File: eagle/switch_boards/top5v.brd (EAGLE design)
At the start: 72.1 x 41.9 mm, 9 parts

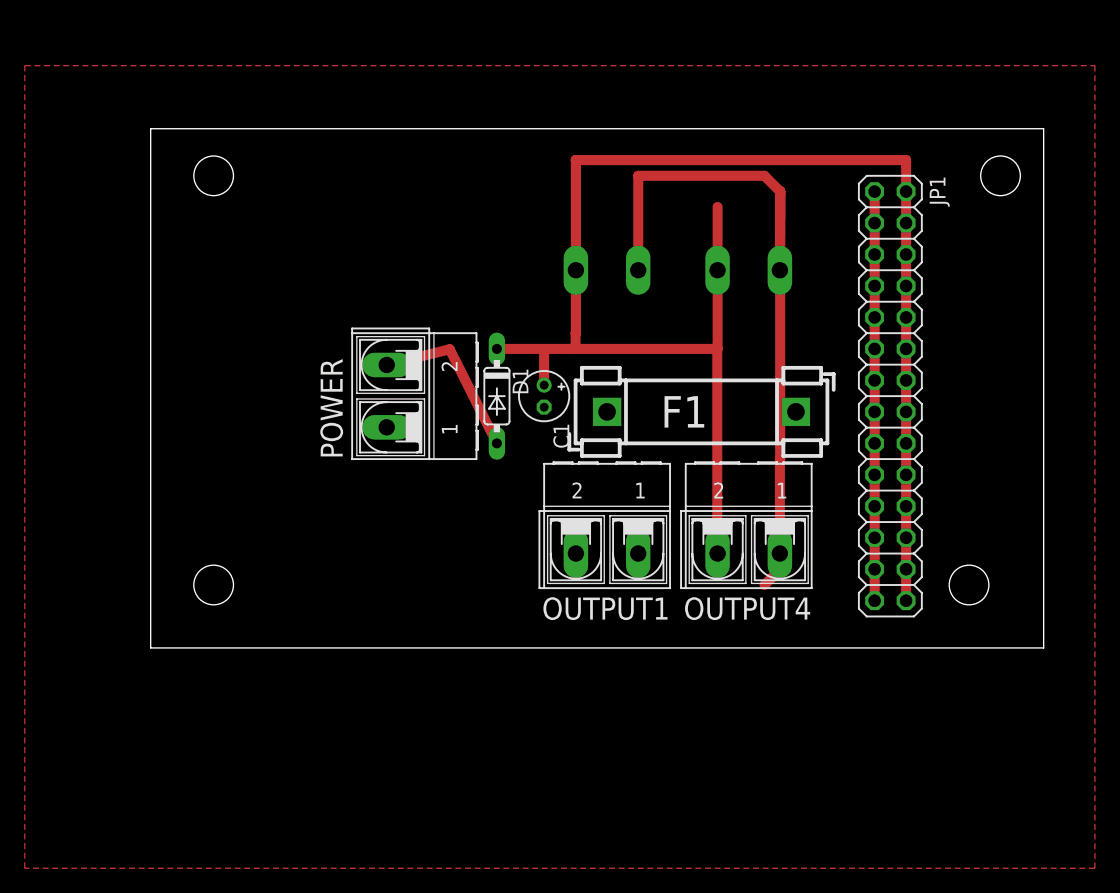
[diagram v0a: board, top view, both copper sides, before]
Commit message: switch board for 5v
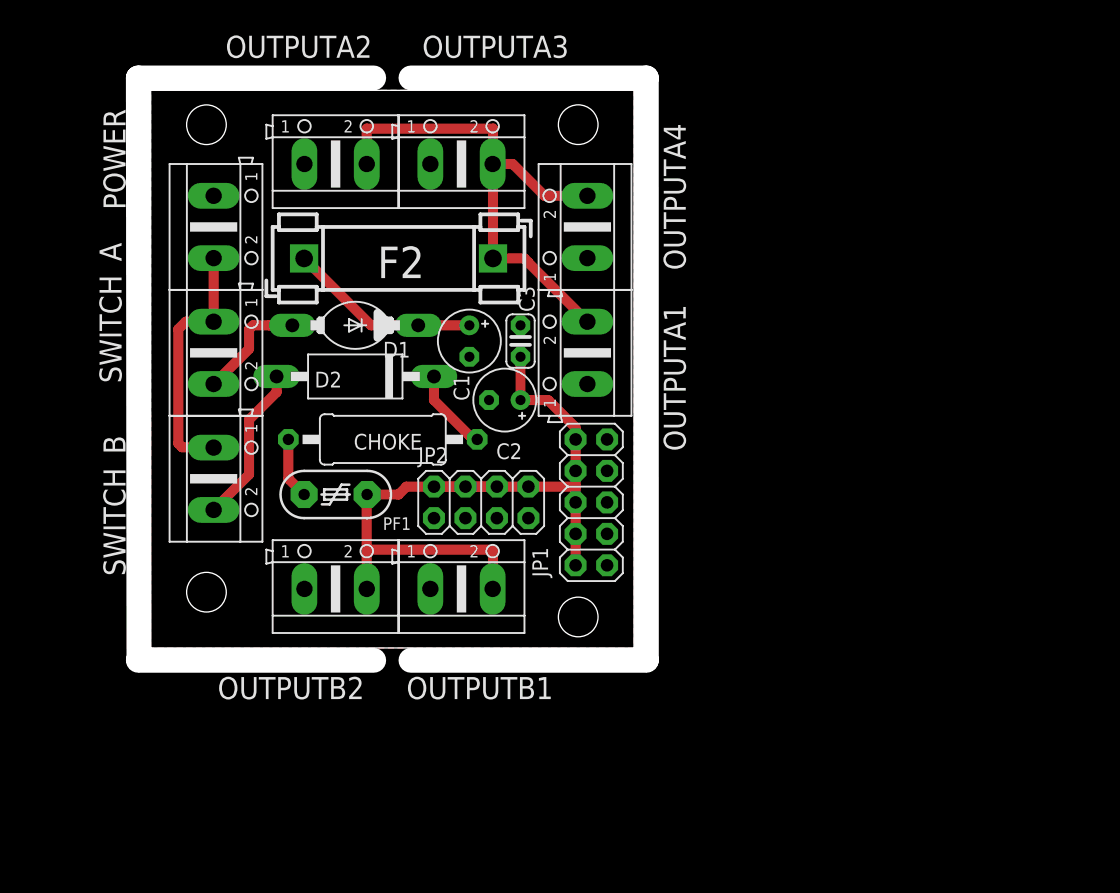
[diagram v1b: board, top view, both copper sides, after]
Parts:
- removed F1: FUSEBLANK_5X20MM, fuse:FUSE_HOLDER_5X20MM
- removed OUTPUT1, OUTPUT2, OUTPUT3, OUTPUT4: 5V, con-ptr500:AK500/2-H
- added C2: (no value), rcl:E2,5-5
- added C3: (no value), resistor:C025-024X044
- added CHOKE: 22uH, resistor:0411/15
- added D2: 1N5060GP, diode:DO15-12
- added F2: FUSEBLANK_5X20MM, fuse:FUSE_HOLDER_5X20MM
- added JP2: (no value), pinhead:2X04
- added OUTPUTA1, OUTPUTA2, OUTPUTA3, OUTPUTA4, OUTPUTB1, OUTPUTB2, SWITCH_A, SWITCH_B: 5V, con-ptr500:AK500/2
- added PF1: PTC-MF-5,1B, polyswitch:MF-5/1B
- C1: device resistor:E1,8-4 -> rcl:E2,5-5
- D1: value 1N4148DO35-7 -> 1N5059; device diode:DO35-7 -> diode:DO204-10
- JP1: device pinhead:2X14 -> pinhead:2X05
- POWER: device con-ptr500:AK500/2-H -> con-ptr500:AK500/2
- moved JP1 25.6 mm to (35.6, 11.7), turned to 90 degrees
- moved POWER 19.5 mm to (5.08, 34.0), turned to 270 degrees
- moved D1 12.8 mm to (16.5, 26.0), turned to 180 degrees
- moved C1 7.49 mm to (25.7, 24.8)
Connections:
- removed net OUTPUT_+5V: C1.+, D1.C, JP1.10, JP1.12, JP1.14, JP1.16, JP1.18, JP1.2, JP1.20, JP1.22, JP1.24, JP1.26, JP1.28, JP1.4, JP1.6, JP1.8, OUTPUT1.2, OUTPUT2.2, OUTPUT3.2, OUTPUT4.2
- removed net OUTPUT_GND: F1.1, JP1.1, JP1.11, JP1.13, JP1.15, JP1.17, JP1.19, JP1.21, JP1.23, JP1.25, JP1.27, JP1.3, JP1.5, JP1.7, JP1.9, OUTPUT1.1, OUTPUT2.1, OUTPUT3.1, OUTPUT4.1
- new net A+5V: D1.A, SWITCH_A.2
- new net B+5V: D2.A, SWITCH_B.2
- new net BRANCH_A_+5V: F2.1, OUTPUTA1.2, OUTPUTA2.2, OUTPUTA3.2, OUTPUTA4.2
- new net BRANCH_B_+5V: C2.+, C3.1, JP1.10, JP1.2, JP1.4, JP1.6, JP1.8, JP2.2, JP2.4, JP2.6, JP2.8, OUTPUTB1.2, OUTPUTB2.2, PF1.2
- new net N$1: CHOKE.1, D2.C
- new net N$12: C1.+, D1.C, F2.2
- new net N$2: CHOKE.2, PF1.1
- net +5V: now also SWITCH_A.1, SWITCH_B.1; no longer D1.A
- net GND: now also C2.-, C3.2, JP1.1, JP1.3, JP1.5, JP1.7, JP1.9, JP2.1, JP2.3, JP2.5, JP2.7, OUTPUTA1.1, OUTPUTA2.1, OUTPUTA3.1, OUTPUTA4.1, OUTPUTB1.1, OUTPUTB2.1; no longer F1.2
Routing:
- net OUTPUT_+5V: track 128.7 -> 0.00 mm
- net OUTPUT_GND: track 98.9 -> 0.00 mm
- net BRANCH_B_+5V: track 0.00 -> 63.2 mm
- net BRANCH_A_+5V: track 0.00 -> 42.0 mm
- net N$12: track 0.00 -> 15.6 mm
- net B+5V: track 0.00 -> 12.9 mm
- net A+5V: track 0.00 -> 11.1 mm
- net +5V: track 13.7 -> 20.4 mm
- net N$1: track 0.00 -> 6.66 mm
- net N$2: track 0.00 -> 4.97 mm
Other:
- board size 72.1 x 41.9 mm -> 41 x 47 mm
